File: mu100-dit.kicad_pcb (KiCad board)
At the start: 2 copper layers, 19.6 x 24 mm, 6 parts, among them J1 Conn_01x05_Male, J2 Conn_01x02_Male, U1 TOTX-177L, U2 AK4103A

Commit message: fix issue with totx177 footprint, fix schematics
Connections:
- U1 pad 1: /TXP -> GND
- U1 pad 3: GND -> /TXP
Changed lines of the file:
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@@
     (fp_rect (start -2.08 -6.14) (end 9.72 4.96) (layer "F.SilkS") (width 0.05) (fill none))
     (fp_rect (start -2.18 -6.24) (end 9.82 5.06) (layer "F.CrtYd") (width 0.05) (fill none))
+    (fp_circle (center 7.63 -1.44) (end 9.34 -1.36) (layer "F.CrtYd") (width 0.05) (fill none))
     (fp_circle (center 0.01 -1.44) (end 1.72 -1.36) (layer "F.CrtYd") (width 0.05) (fill none))
-    (fp_circle (center 7.63 -1.44) (end 9.34 -1.36) (layer "F.CrtYd") (width 0.05) (fill none))
+    (pad "" np_thru_hole circle (at 7.63 -1.44 270) (size 3.2 3.2) (drill 3.2) (layers *.Cu *.Mask))
     (pad "" np_thru_hole circle (at 0.01 -1.44 270) (size 3.2 3.2) (drill 3.2) (layers *.Cu *.Mask))
-    (pad "" np_thru_hole circle (at 7.63 -1.44 270) (size 3.2 3.2) (drill 3.2) (layers *.Cu *.Mask))
-    (pad "1" thru_hole circle (at 6.36 2.37 270) (size 1.524 1.524) (drill 0.8) (layers *.Cu *.Mask)
-      (net 11 "/TXP") (pinfunction "GND") (pintype "input"))
+    (pad "1" thru_hole circle (at 1.28 2.37 270) (size 1.524 1.524) (drill 0.8) (layers *.Cu *.Mask)
+      (net 1 "GND") (pinfunction "GND") (pintype "input"))
     (pad "2" thru_hole circle (at 3.82 2.37 270) (size 1.524 1.524) (drill 0.8) (layers *.Cu *.Mask)
       (net 2 "+5V") (pinfunction "VCC") (pintype "input"))
-    (pad "3" thru_hole circle (at 1.28 2.37 270) (size 1.524 1.524) (drill 0.8) (layers *.Cu *.Mask)
-      (net 1 "GND") (pinfunction "Input") (pintype "input"))
-    (model "${KIPRJMOD}/footprints/User Library-TORX147L-1.STEP"
-      (offset (xyz 3.8 6.25 5))
+    (pad "3" thru_hole circle (at 6.36 2.37 270) (size 1.524 1.524) (drill 0.8) (layers *.Cu *.Mask)
+      (net 11 "/TXP") (pinfunction "Input") (pintype "input"))
+    (model "${KICAD6_3DMODEL_DIR}/OptoDevice.3dshapes/Toshiba_TOTX170_TOTX173_TOTX193_TOTX194.wrl"
+      (offset (xyz 0 0 0))
       (scale (xyz 1 1 1))
-      (rotate (xyz 0 0 180))
+      (rotate (xyz 0 0 0))
     )
   )

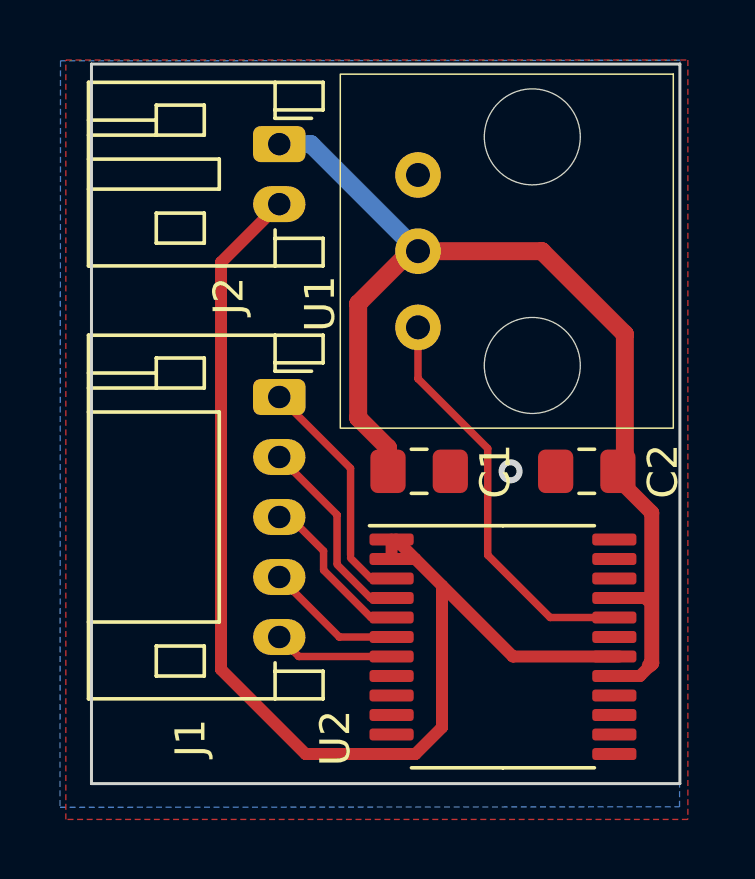
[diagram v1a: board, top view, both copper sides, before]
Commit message: add jumpers to board
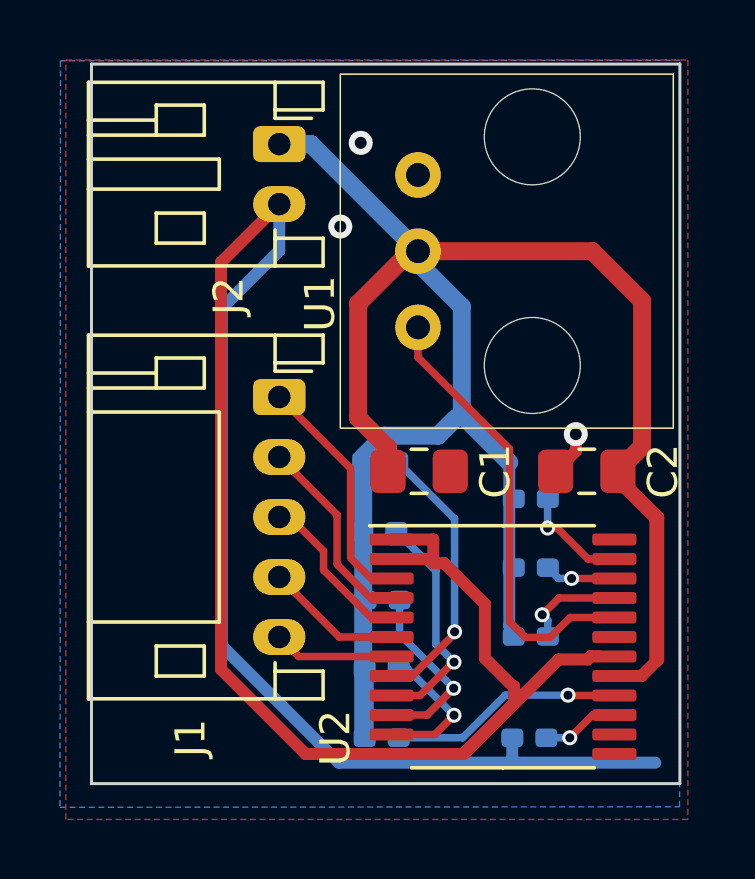
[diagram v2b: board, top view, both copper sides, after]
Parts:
- added JP1: Jumper_NO_Small, Capacitor_SMD:C_0402_1005Metric_Pad0.74x0.62mm_HandSolder, B.Cu at (51.3, 106.9)
- added JP2: Jumper_NO_Small, Capacitor_SMD:C_0402_1005Metric_Pad0.74x0.62mm_HandSolder, B.Cu at (51.2, 109.2)
- added JP3: Jumper_NO_Small, Capacitor_SMD:C_0402_1005Metric_Pad0.74x0.62mm_HandSolder, B.Cu at (51.4, 111.5)
- added JP4: Jumper_NO_Small, Capacitor_SMD:C_0402_1005Metric_Pad0.74x0.62mm_HandSolder, B.Cu at (51.3, 113.8)
- added JP5: Jumper_NO_Small, Capacitor_SMD:C_0402_1005Metric_Pad0.74x0.62mm_HandSolder, B.Cu at (56.3, 112.7)
- added JP6: Jumper_NO_Small, Capacitor_SMD:C_0402_1005Metric_Pad0.74x0.62mm_HandSolder, B.Cu at (56.3, 110.4)
- added JP7: Jumper_NO_Small, Capacitor_SMD:C_0402_1005Metric_Pad0.74x0.62mm_HandSolder, B.Cu at (56.3, 108.1)
- added JP8: Jumper_NO_Small, Capacitor_SMD:C_0402_1005Metric_Pad0.74x0.62mm_HandSolder, B.Cu at (56.2, 116.1)
- added JP9: Jumper_NO_Small, Capacitor_SMD:C_0402_1005Metric_Pad0.74x0.62mm_HandSolder, B.Cu at (51.3, 116.1)
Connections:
- U2 pad 10: unconnected-(U2-Pad10) -> /FS2
- U2 pad 11: unconnected-(U2-Pad11) -> /FS3
- U2 pad 15: unconnected-(U2-Pad15) -> /CKS0
- U2 pad 16: unconnected-(U2-Pad16) -> /CKS1
- U2 pad 21: +5V -> /DIF0
- U2 pad 22: unconnected-(U2-Pad22) -> /DIF1
- U2 pad 23: unconnected-(U2-Pad23) -> /DIF2
- U2 pad 8: unconnected-(U2-Pad8) -> /FS0
- U2 pad 9: unconnected-(U2-Pad9) -> /FS1
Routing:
- net GND: track 40.5 -> 77.5 mm, vias 1 -> 3
- net +5V: track 36.4 -> 66.1 mm
- net /FS0: track 0.00 -> 9.22 mm, vias 0 -> 1
- net /CKS1: track 0.00 -> 7.78 mm, vias 0 -> 1
- net /FS1: track 0.00 -> 7.70 mm, vias 0 -> 1
- net /FS2: track 0.00 -> 6.13 mm, vias 0 -> 1
- net /FS3: track 0.00 -> 4.83 mm, vias 0 -> 1
- net /DIF2: track 0.00 -> 3.63 mm, vias 0 -> 1
- net /DIF0: track 0.00 -> 3.44 mm, vias 0 -> 1
- net /CKS0: track 0.00 -> 2.58 mm, vias 0 -> 1
- net /DIF1: track 0.00 -> 2.37 mm, vias 0 -> 1
- net /TXP: track 13.6 -> 15.1 mm
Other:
- board text added: "(PDWN)"
- board text added: "CKS0"
- board text added: "CKS1"
- board text added: "DIF0"
- board text added: "DIF1"
- board text added: "DIF2"
- board text added: "FS0"
- board text added: "FS1"
- board text added: "FS2"
- board text added: "FS3"
